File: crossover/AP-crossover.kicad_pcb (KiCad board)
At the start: 2 copper layers, 92.5 x 50 mm, 99 parts, among them U1 OPA1604, U2 OPA1604, U3 LM317_TO-252, U4 LM337_TO252, X1 PinHeader_1x02_P2.54mm_Vertic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, X2 PinHeader_1x02_P2.54mm_Vertic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, X3 PinHeader_1x02_P2.54mm_Vertic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, X4 PinHeader_1x02_P2.54mm_Vertic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

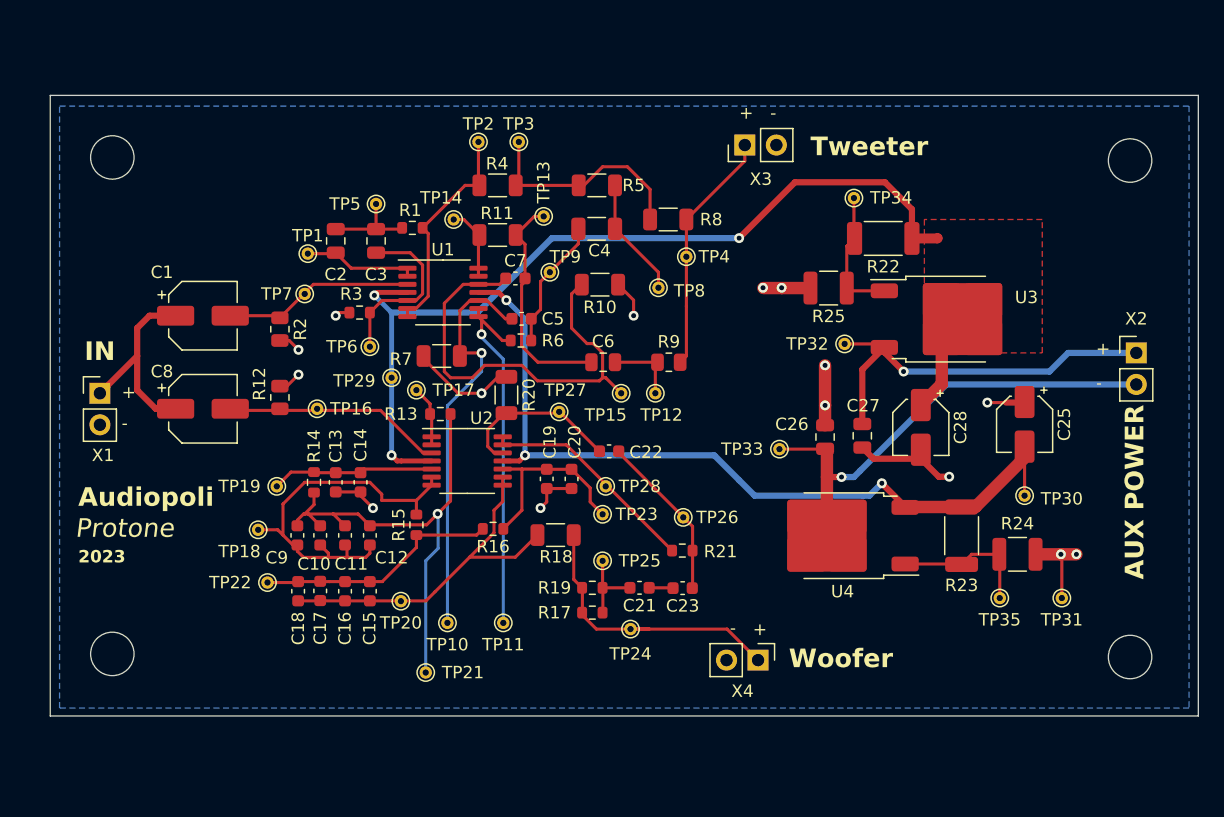
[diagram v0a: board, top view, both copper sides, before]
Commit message: Update pcb layout to revision B, add balanced input
Co-Authored-By: ithinkido <52834821+ithinkido@users.noreply.github.com>
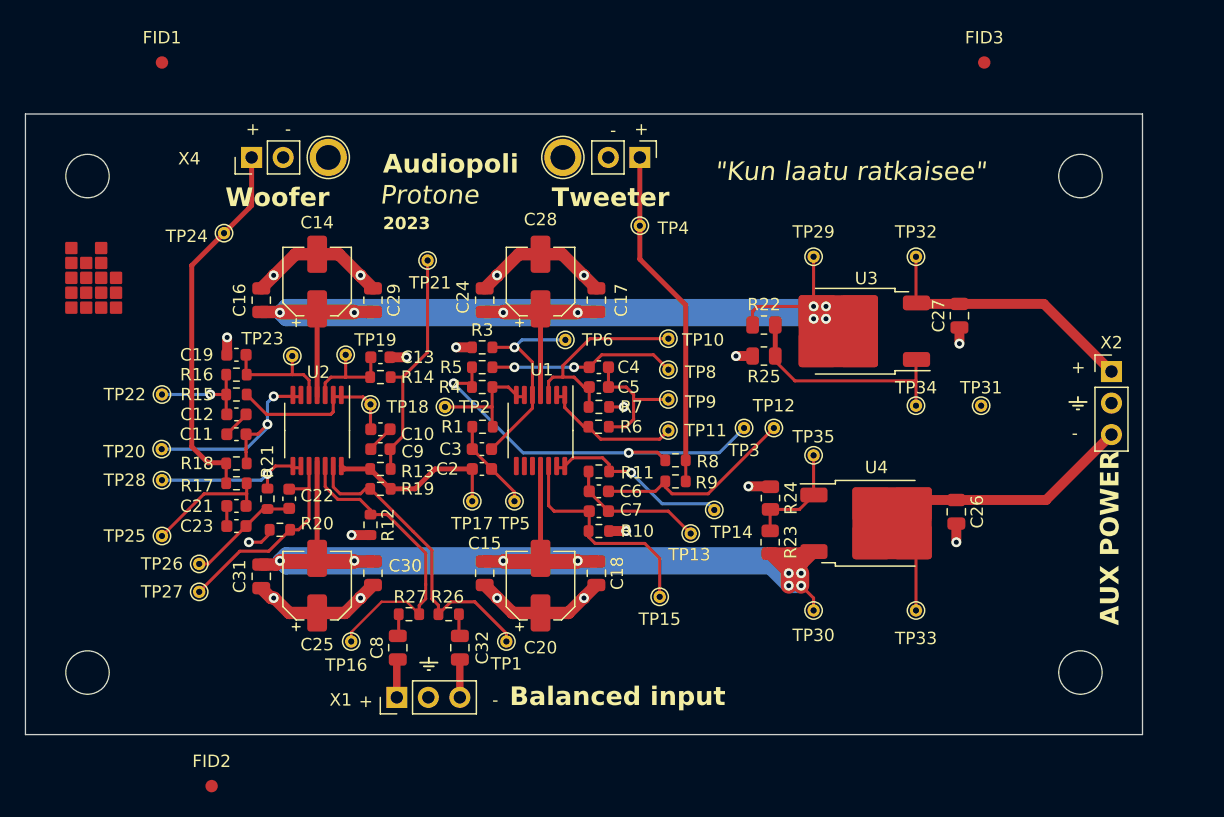
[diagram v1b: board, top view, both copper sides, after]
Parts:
- removed C1: 1.2u, Capacitor_SMD:CP_Elec_5x5.7
- removed R2: 21.5k, Resistor_SMD:R_0805_2012Metric
- removed TP7: TestPoint, TestPoint:TestPoint_THTPad_D1.0mm_Drill0.5mm
- added C24: 100n, Capacitor_SMD:C_0805_2012Metric, F.Cu at (155.0, 91.0)
- added C29: 100n, Capacitor_SMD:C_0805_2012Metric, F.Cu at (146.0, 91.0)
- added C30: 100n, Capacitor_SMD:C_0805_2012Metric, F.Cu at (146.0, 113.0)
- added C31: 100n, Capacitor_SMD:C_0805_2012Metric, F.Cu at (137.0, 113.2)
- added C32: 1u, Capacitor_SMD:C_0805_2012Metric, F.Cu at (153.0, 119.0)
- added FID1: Fiducial_1mm_Mask2mm, Fiducial:Fiducial_1mm_Mask2mm, F.Cu at (129.0, 71.8)
- added FID2: Fiducial_1mm_Mask2mm, Fiducial:Fiducial_1mm_Mask2mm, F.Cu at (133.0, 130.2)
- added FID3: Fiducial_1mm_Mask2mm, Fiducial:Fiducial_1mm_Mask2mm, F.Cu at (195.2, 71.8)
- added R26: 10k, Resistor_SMD:R_0603_1608Metric, F.Cu at (152.1, 116.3)
- added R27: 10k, Resistor_SMD:R_0603_1608Metric, F.Cu at (148.9, 116.3)
- added REF**: TestPoint_Plated_Hole_D2.0mm, TestPoint:TestPoint_Plated_Hole_D2.0mm, F.Cu at (161.3, 79.5)
- added REF**: TestPoint_Plated_Hole_D2.0mm, TestPoint:TestPoint_Plated_Hole_D2.0mm, F.Cu at (142.4, 79.5)
- C10, C11, C12, C9: value 27n -> 220n
- C13, C19: value 27n -> 56n
- C14, C15: value 27n -> 10u; footprint Capacitor_SMD:C_0603_1608Metric -> Capacitor_SMD:CP_Elec_5x5.4
- C16, C17, C18, C20: value 27n -> 100n; footprint Capacitor_SMD:C_0603_1608Metric -> Capacitor_SMD:C_0805_2012Metric
- C2, C3, C6: footprint Capacitor_SMD:C_0805_2012Metric -> Capacitor_SMD:C_0603_1608Metric
- C25, C28: value 1u -> 10u; footprint Capacitor_SMD:CP_Elec_4x5.4 -> Capacitor_SMD:CP_Elec_5x5.4
- C4: footprint Capacitor_SMD:C_1206_3216Metric -> Capacitor_SMD:C_0603_1608Metric
- C8: value 1.2u -> 1u; footprint Capacitor_SMD:CP_Elec_5x5.7 -> Capacitor_SMD:C_0805_2012Metric
- R10, R20, R7: footprint Resistor_SMD:R_1206_3216Metric -> Resistor_SMD:R_0603_1608Metric
- R11: value 121 -> 120; footprint Resistor_SMD:R_1206_3216Metric -> Resistor_SMD:R_0603_1608Metric
- R12: value 21.5k -> 10k; footprint Resistor_SMD:R_0805_2012Metric -> Resistor_SMD:R_0603_1608Metric
- R17: value 1.62k -> 820
- R18, R4, R5: value 1.02k -> 1k; footprint Resistor_SMD:R_1206_3216Metric -> Resistor_SMD:R_0603_1608Metric
- R19: value 1.62k -> 10k
- R22, R23: value 240 -> 470; footprint Resistor_SMD:R_2010_5025Metric -> Resistor_SMD:R_0805_2012Metric
- R24, R25: value 2.6k -> 2.2k; footprint Resistor_SMD:R_1210_3225Metric -> Resistor_SMD:R_0805_2012Metric
- R8: value 1.02k -> 1.5k; footprint Resistor_SMD:R_1206_3216Metric -> Resistor_SMD:R_0603_1608Metric
- R9: footprint Resistor_SMD:R_0805_2012Metric -> Resistor_SMD:R_0603_1608Metric
- X1, X2: value PinHeader_1x02_P2.54mm_Vertical -> PinHeader_1x03_P2.54mm_Vertical; footprint Connector_PinHeader_2.54mm:PinHeader_1x02_P2.54mm_Vertical -> Connector_PinHeader_2.54mm:PinHeader_1x03_P2.54mm_Vertical
- moved C25 58.5 mm to (141.5, 114.0), turned to 90 degrees
- moved X4 57.5 mm to (136.2, 79.5), turned to 90 degrees
- moved TP24 45.7 mm to (134.0, 85.6)
- moved TP26 39.2 mm to (132.0, 112.2)
- moved C23 36.3 mm to (135.0, 109.2)
- moved TP28 35.8 mm to (129.0, 105.5)
- moved TP25 35.6 mm to (129.0, 110.0)
- moved TP29 35.4 mm to (181.5, 87.5)
- moved TP1 35.1 mm to (156.8, 118.5)
- moved X1 34.2 mm to (147.9, 123.0), turned to 90 degrees
- moved R21 33.7 mm to (137.5, 107.0), turned to 90 degrees
- moved TP21 33.2 mm to (150.4, 87.8)
- moved C21 33.1 mm to (135.0, 107.6), turned to 0 degrees
- moved C28 32.8 mm to (159.5, 89.5), turned to 90 degrees
- moved TP27 32.4 mm to (132.0, 114.5)
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- renumbered REF** to H1, REF** to H2, REF** to H3, REF** to H4
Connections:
- C10 pad 2: Net-(U2B--) -> Net-(U2A--)
- C11 pad 1: Net-(C10-Pad1) -> Net-(C11-Pad1)
- C11 pad 2: Net-(U2B--) -> /CrossW
- C12 pad 1: Net-(C10-Pad1) -> Net-(C12-Pad1)
- C12 pad 2: Net-(U2B--) -> Net-(C11-Pad1)
- C13 pad 2: Net-(U2B-+) -> Net-(U2A-+)
- C14 pad 1: GND -> VDD
- C14 pad 2: Net-(U2B-+) -> GND
- C15 pad 1: Net-(C15-Pad1) -> GND
- C15 pad 2: /CrossW -> VSS
- C16 pad 1: Net-(C15-Pad1) -> GND
- C16 pad 2: /CrossW -> VDD
- C17 pad 1: Net-(C15-Pad1) -> GND
- C17 pad 2: /CrossW -> VDD
- C18 pad 1: Net-(C15-Pad1) -> VSS
- C18 pad 2: /CrossW -> GND
- C19 pad 2: Net-(U2C-+) -> Net-(U2B-+)
- C2 pad 1: Net-(U1A--) -> Net-(C2-Pad1)
- C20 pad 1: GND -> VSS
- C20 pad 2: Net-(U2C-+) -> GND
- C22 pad 1: Net-(U2D-+) -> Net-(U2C-+)
- C25 pad 2: -15V -> VSS
- C28 pad 1: +15V -> VDD
- C5 pad 1: Net-(U1C-+) -> Net-(U1A-+)
- C8 pad 2: Net-(U2A-+) -> Net-(C8-Pad2)
- C9 pad 1: Net-(C10-Pad1) -> Net-(C9-Pad1)
- C9 pad 2: Net-(U2B--) -> Net-(C10-Pad1)
- R12 pad 1: Net-(U2A-+) -> /BINP
- R13 pad 1: Net-(C10-Pad1) -> Net-(C9-Pad1)
- R13 pad 2: Net-(U2A--) -> Net-(C2-Pad1)
- R14 pad 1: Net-(U2B-+) -> Net-(U2A-+)
- R14 pad 2: Net-(C10-Pad1) -> Net-(C9-Pad1)
- R15 pad 1: Net-(C15-Pad1) -> Net-(C12-Pad1)
- R15 pad 2: Net-(U2B--) -> Net-(U2A--)
- R16 pad 1: Net-(U2C-+) -> Net-(U2B-+)
- R16 pad 2: Net-(C15-Pad1) -> Net-(C12-Pad1)
- R19 pad 1: Net-(C21-Pad2) -> /BINN
- R19 pad 2: WOUT -> Net-(C2-Pad1)
- R20 pad 2: Net-(U2D-+) -> Net-(U2C-+)
- R21 pad 2: Net-(U2D--) -> Net-(U2C--)
- R22 pad 1: +15V -> VDD
- R23 pad 2: -15V -> VSS
- R6 pad 2: Net-(U1C--) -> Net-(U1A--)
- R7 pad 2: Net-(U1C-+) -> Net-(U1A-+)
- TP1 pad 1: Net-(U1A--) -> /BINN
- TP10 pad 1: Net-(U1C-+) -> Net-(U1A-+)
- TP11 pad 1: Net-(U1C--) -> Net-(U1A--)
- TP16 pad 1: Net-(U2A-+) -> /BINP
- TP17 pad 1: Net-(U2A--) -> Net-(C2-Pad1)
- TP18 pad 1: Net-(U2B--) -> Net-(U2A--)
- TP19 pad 1: Net-(U2B-+) -> Net-(U2A-+)
- TP21 pad 1: Net-(C10-Pad1) -> Net-(C9-Pad1)
- TP22 pad 1: Net-(C15-Pad1) -> Net-(C12-Pad1)
- TP23 pad 1: Net-(U2C-+) -> Net-(U2B-+)
- TP27 pad 1: Net-(U2D-+) -> Net-(U2C-+)
- TP28 pad 1: Net-(U2D--) -> Net-(U2C--)
- TP29 pad 1: +15V -> VDD
- TP30 pad 1: -15V -> VSS
- U1 pad 10: Net-(U1C-+) -> (no net)
- U1 pad 11: -15V -> VSS
- U1 pad 4: +15V -> VDD
- U1 pad 8: Net-(U1C--) -> (no net)
- U1 pad 9: Net-(U1C--) -> (no net)
- U2 pad 11: -15V -> VSS
- U2 pad 12: Net-(U2D-+) -> /BINP
- U2 pad 13: Net-(U2D--) -> /BINN
- U2 pad 14: Net-(U2D--) -> Net-(C2-Pad1)
- U2 pad 4: +15V -> VDD
- U2 pad 6: Net-(U2B--) -> /CrossW
- U2 pad 7: Net-(U2B--) -> /CrossW
- U2 pad 8: /CrossW -> Net-(U2C--)
- U2 pad 9: /CrossW -> Net-(U2C--)
- U3 pad 2: +15V -> VDD
- U4 pad 3: -15V -> VSS
- X2 pad 2: -24V -> GND
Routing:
- net VSS: track 0.00 -> 133.9 mm, vias 0 -> 8
- net VDD: track 0.00 -> 131.5 mm, vias 0 -> 8
- net +15V: track 77.3 -> 0.00 mm, vias 3 -> 0
- net -15V: track 65.0 -> 0.00 mm, vias 3 -> 0
- net Net-(C10-Pad1): track 39.2 -> 2.24 mm, vias 1 -> 0
- net Net-(U1C-+): track 33.6 -> 0.00 mm, vias 1 -> 0
- net Net-(U2B--): track 31.8 -> 0.00 mm
- net Net-(U1C--): track 29.6 -> 0.00 mm, vias 1 -> 0
- net /BINN: track 0.00 -> 25.0 mm
- net /BINP: track 0.00 -> 25.0 mm
- net Net-(C15-Pad1): track 19.7 -> 0.00 mm
- net Net-(C9-Pad1): track 0.00 -> 19.0 mm
- net Net-(U1D-+): track 36.5 -> 18.3 mm
- net Net-(U2D--): track 17.8 -> 0.00 mm
- net -24V: track 39.0 -> 23.9 mm, vias 1 -> 0
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- added copper zone on In1.Cu, net GND
- added copper zone on In2.Cu, net GND
- removed copper zone on F.Cu, net +15V
- removed copper zone on B.Cu, net GND
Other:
- board size 92.5 x 50 mm -> 90 x 50 mm
- copper layers 2 -> 4
- board text added: "17.4.2023"
- board text added: "B"
- board text added: "Balanced input"
- board text added: "F.Cu - front copper B.Cu - back copper F.Adhesive - front adhesive B.Adhesive - Back adhesive F.Paste - front solder paste B.Paste - back solder paste User.Drawings - non-important information User.Comments - non-important information User.Eco1 - User.Eco2 - Edge.Cuts - Board outline Margin - Component margins F.Courtyard - Front courtyard B.Courtyard - Back courtyard User.1 - Layer information U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"
- board text added: "LR2"
- board text added: "LR4"
- board text added: "Layer definitions"
- board text added: "V-Cut"
- board text added: "f 1400 Hz"
- board text added: "f 2530 Hz A -5.7 dB Q 1"
- board text added: "f 6000 Hz A -2 dB Q 2.4"
- board text added: "f 770 Hz A -6 dB Q 2.3"
- board text added: "f 860 Hz"
- board text added: "for unbalanced input, solder gnd and - together"
- board text added: "in"
- board text added: "{dblquote}Kun laatu ratkaisee{dblquote}"
- board text removed: "IN"

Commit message: Add git hub action to create board preview.
Also clean up Tiltle block so that the svg export works correct
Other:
- board text removed: "17.4.2023"
- board text removed: "Active crossover for Audiopoli Protone speakers"
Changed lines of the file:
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@@
   )
   (paper "A4")
+  (title_block
+    (title "Active crossover for Audiopoli Protone speakers\n")
+    (date "2023-05-06")
+    (rev "B")
+  )
   (layers
     (0 "F.Cu" signal)
@@
     (effects (font (size 1.5 1.5) (thickness 0.3) bold) (justify left bottom))
   )
-  (gr_text "17.4.2023\n" (at 206.75 194) (layer "Dwgs.User")
-    (effects (font (size 1.5 1.5) (thickness 0.3) bold) (justify left bottom))
-  )
-  (gr_text "Active crossover for Audiopoli Protone speakers\n" (at 187.25 190.25) (layer "User.1")
-    (effects (font (size 1.5 1.5) (thickness 0.3) bold) (justify left bottom))
-  )

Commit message: Update AP-crossover.kicad_pcb
Change visabiliy of comment layer to fix scaling of svg export
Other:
- board text removed: "B"
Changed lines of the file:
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@@
     (fp_line (start 1 0.625) (end -1 0.625)
       (stroke (width 0.1) (type solid)) (layer "F.Fab"))
-    (pad "1" smd roundrect (at -0.9125 0) (size 1.025 1.4) (layers "F.Cu" "F.Paste" "F.Mask") (roundrect_rratio 0.243902)
+    (pad "1" smd roundrect (at -0.9125 0) (size 1.025 1.4) (layers "F.Cu" "F.Paste" "F.Mask") (roundrect_rratio 0.243902439)
       (net 29 "VDD") (pintype "passive"))
-    (pad "2" smd roundrect (at 0.9125 0) (size 1.025 1.4) (layers "F.Cu" "F.Paste" "F.Mask") (roundrect_rratio 0.243902)
+    (pad "2" smd roundrect (at 0.9125 0) (size 1.025 1.4) (layers "F.Cu" "F.Paste" "F.Mask") (roundrect_rratio 0.243902439)
       (net 33 "Net-(U3-ADJ)") (pintype "passive"))
     (model "${KICAD6_3DMODEL_DIR}/Resistor_SMD.3dshapes/R_0805_2012Metric.wrl"
@@
     (fp_line (start 1 0.625) (end -1 0.625)
       (stroke (width 0.1) (type solid)) (layer "F.Fab"))
-    (pad "1" smd roundrect (at -0.9125 0 180) (size 1.025 1.4) (layers "F.Cu" "F.Paste" "F.Mask") (roundrect_rratio 0.243902)
+    (pad "1" smd roundrect (at -0.9125 0 180) (size 1.025 1.4) (layers "F.Cu" "F.Paste" "F.Mask") (roundrect_rratio 0.243902439)
       (net 33 "Net-(U3-ADJ)") (pintype "passive"))
-    (pad "2" smd roundrect (at 0.9125 0 180) (size 1.025 1.4) (layers "F.Cu" "F.Paste" "F.Mask") (roundrect_rratio 0.243902)
+    (pad "2" smd roundrect (at 0.9125 0 180) (size 1.025 1.4) (layers "F.Cu" "F.Paste" "F.Mask") (roundrect_rratio 0.243902439)
       (net 13 "GND") (pintype "passive"))
     (model "${KICAD6_3DMODEL_DIR}/Resistor_SMD.3dshapes/R_0805_2012Metric.wrl"
@@
     (fp_line (start 1 0.625) (end -1 0.625)
       (stroke (width 0.1) (type solid)) (layer "F.Fab"))
-    (pad "1" smd roundrect (at -0.9125 0 270) (size 1.025 1.4) (layers "F.Cu" "F.Paste" "F.Mask") (roundrect_rratio 0.243902)
+    (pad "1" smd roundrect (at -0.9125 0 270) (size 1.025 1.4) (layers "F.Cu" "F.Paste" "F.Mask") (roundrect_rratio 0.243902439)
       (net 13 "GND") (pintype "passive"))
-    (pad "2" smd roundrect (at 0.9125 0 270) (size 1.025 1.4) (layers "F.Cu" "F.Paste" "F.Mask") (roundrect_rratio 0.243902)
+    (pad "2" smd roundrect (at 0.9125 0 270) (size 1.025 1.4) (layers "F.Cu" "F.Paste" "F.Mask") (roundrect_rratio 0.243902439)
       (net 34 "Net-(U4-ADJ)") (pintype "passive"))
     (model "${KICAD6_3DMODEL_DIR}/Resistor_SMD.3dshapes/R_0805_2012Metric.wrl"
@@
     (fp_line (start 4.11 2.7) (end 3.11 2.7)
       (stroke (width 0.1) (type solid)) (layer "F.Fab"))
-    (pad "1" smd roundrect (at -5.04 -2.28 180) (size 2.2 1.2) (layers "F.Cu" "F.Paste" "F.Mask") (roundrect_rratio 0.208333)
+    (pad "1" smd roundrect (at -5.04 -2.28 180) (size 2.2 1.2) (layers "F.Cu" "F.Paste" "F.Mask") (roundrect_rratio 0.2083333333)
       (net 33 "Net-(U3-ADJ)") (pinfunction "ADJ") (pintype "input"))
-    (pad "2" smd roundrect (at -0.415 -1.525 180) (size 3.05 2.75) (layers "F.Cu" "F.Paste") (roundrect_rratio 0.090909)
+    (pad "2" smd roundrect (at -0.415 -1.525 180) (size 3.05 2.75) (layers "F.Cu" "F.Paste") (roundrect_rratio 0.09090909091)
       (net 29 "VDD") (pinfunction "VO") (pintype "power_out"))
-    (pad "2" smd roundrect (at -0.415 1.525 180) (size 3.05 2.75) (layers "F.Cu" "F.Paste") (roundrect_rratio 0.090909)
+    (pad "2" smd roundrect (at -0.415 1.525 180) (size 3.05 2.75) (layers "F.Cu" "F.Paste") (roundrect_rratio 0.09090909091)
       (net 29 "VDD") (pinfunction "VO") (pintype "power_out"))
-    (pad "2" smd roundrect (at 1.26 0 180) (size 6.4 5.8) (layers "F.Cu" "F.Mask") (roundrect_rratio 0.043103)
+    (pad "2" smd roundrect (at 1.26 0 180) (size 6.4 5.8) (layers "F.Cu" "F.Mask") (roundrect_rratio 0.04310293103)
       (net 29 "VDD") (pinfunction "VO") (pintype "power_out"))
-    (pad "2" smd roundrect (at 2.935 -1.525 180) (size 3.05 2.75) (layers "F.Cu" "F.Paste") (roundrect_rratio 0.090909)
+    (pad "2" smd roundrect (at 2.935 -1.525 180) (size 3.05 2.75) (layers "F.Cu" "F.Paste") (roundrect_rratio 0.09090909091)
       (net 29 "VDD") (pinfunction "VO") (pintype "power_out"))
-    (pad "2" smd roundrect (at 2.935 1.525 180) (size 3.05 2.75) (layers "F.Cu" "F.Paste") (roundrect_rratio 0.090909)
+    (pad "2" smd roundrect (at 2.935 1.525 180) (size 3.05 2.75) (layers "F.Cu" "F.Paste") (roundrect_rratio 0.09090909091)
       (net 29 "VDD") (pinfunction "VO") (pintype "power_out"))
-    (pad "3" smd roundrect (at -5.04 2.28 180) (size 2.2 1.2) (layers "F.Cu" "F.Paste" "F.Mask") (roundrect_rratio 0.208333)
+    (pad "3" smd roundrect (at -5.04 2.28 180) (size 2.2 1.2) (layers "F.Cu" "F.Paste" "F.Mask") (roundrect_rratio 0.2083333333)
       (net 31 "+24V") (pinfunction "VI") (pintype "power_in"))
     (model "${KICAD6_3DMODEL_DIR}/Package_TO_SOT_SMD.3dshapes/TO-252-2.wrl"
@@
     (fp_line (start 1 0.625) (end -1 0.625)
       (stroke (width 0.1) (type solid)) (layer "F.Fab"))
-    (pad "1" smd roundrect (at -0.9125 0 270) (size 1.025 1.4) (layers "F.Cu" "F.Paste" "F.Mask") (roundrect_rratio 0.243902)
+    (pad "1" smd roundrect (at -0.9125 0 270) (size 1.025 1.4) (layers "F.Cu" "F.Paste" "F.Mask") (roundrect_rratio 0.243902439)
       (net 34 "Net-(U4-ADJ)") (pintype "passive"))
-    (pad "2" smd roundrect (at 0.9125 0 270) (size 1.025 1.4) (layers "F.Cu" "F.Paste" "F.Mask") (roundrect_rratio 0.243902)
+    (pad "2" smd roundrect (at 0.9125 0 270) (size 1.025 1.4) (layers "F.Cu" "F.Paste" "F.Mask") (roundrect_rratio 0.243902439)
       (net 32 "VSS") (pintype "passive"))
     (model "${KICAD6_3DMODEL_DIR}/Resistor_SMD.3dshapes/R_0805_2012Metric.wrl"
@@
     (fp_line (start 4.11 2.7) (end 3.11 2.7)
       (stroke (width 0.1) (type solid)) (layer "F.Fab"))
-    (pad "1" smd roundrect (at -5.04 -2.28) (size 2.2 1.2) (layers "F.Cu" "F.Paste" "F.Mask") (roundrect_rratio 0.208333)
+    (pad "1" smd roundrect (at -5.04 -2.28) (size 2.2 1.2) (layers "F.Cu" "F.Paste" "F.Mask") (roundrect_rratio 0.2083333333)
       (net 34 "Net-(U4-ADJ)") (pinfunction "ADJ") (pintype "input"))
-    (pad "2" smd roundrect (at -0.415 -1.525) (size 3.05 2.75) (layers "F.Cu" "F.Paste") (roundrect_rratio 0.090909)
+    (pad "2" smd roundrect (at -0.415 -1.525) (size 3.05 2.75) (layers "F.Cu" "F.Paste") (roundrect_rratio 0.09090909091)
       (net 30 "-24V") (pinfunction "VI") (pintype "power_in"))
-    (pad "2" smd roundrect (at -0.415 1.525) (size 3.05 2.75) (layers "F.Cu" "F.Paste") (roundrect_rratio 0.090909)
+    (pad "2" smd roundrect (at -0.415 1.525) (size 3.05 2.75) (layers "F.Cu" "F.Paste") (roundrect_rratio 0.09090909091)
       (net 30 "-24V") (pinfunction "VI") (pintype "power_in"))
-    (pad "2" smd roundrect (at 1.26 0) (size 6.4 5.8) (layers "F.Cu" "F.Mask") (roundrect_rratio 0.043103)
+    (pad "2" smd roundrect (at 1.26 0) (size 6.4 5.8) (layers "F.Cu" "F.Mask") (roundrect_rratio 0.04310293103)
       (net 30 "-24V") (pinfunction "VI") (pintype "power_in"))
-    (pad "2" smd roundrect (at 2.935 -1.525) (size 3.05 2.75) (layers "F.Cu" "F.Paste") (roundrect_rratio 0.090909)
+    (pad "2" smd roundrect (at 2.935 -1.525) (size 3.05 2.75) (layers "F.Cu" "F.Paste") (roundrect_rratio 0.09090909091)
       (net 30 "-24V") (pinfunction "VI") (pintype "power_in"))
-    (pad "2" smd roundrect (at 2.935 1.525) (size 3.05 2.75) (layers "F.Cu" "F.Paste") (roundrect_rratio 0.090909)
+    (pad "2" smd roundrect (at 2.935 1.525) (size 3.05 2.75) (layers "F.Cu" "F.Paste") (roundrect_rratio 0.09090909091)
       (net 30 "-24V") (pinfunction "VI") (pintype "power_in"))
-    (pad "3" smd roundrect (at -5.04 2.28) (size 2.2 1.2) (layers "F.Cu" "F.Paste" "F.Mask") (roundrect_rratio 0.208333)
+    (pad "3" smd roundrect (at -5.04 2.28) (size 2.2 1.2) (layers "F.Cu" "F.Paste" "F.Mask") (roundrect_rratio 0.2083333333)
       (net 32 "VSS") (pinfunction "VO") (pintype "power_out"))
     (model "${KICAD6_3DMODEL_DIR}/Package_TO_SOT_SMD.3dshapes/TO-252-2.wrl"
@@
     (effects (font (size 1 1) (thickness 0.15)) (justify left bottom))
   )
-  (gr_text "B" (at 269 194) (layer "Dwgs.User")
-    (effects (font (size 1.5 1.5) (thickness 0.3) bold) (justify left bottom))
-  )
   (gr_text "Layer definitions" (at 50.5 79.25) (layer "User.1")
